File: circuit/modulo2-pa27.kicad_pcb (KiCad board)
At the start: 2 copper layers, 100 x 48 mm, 47 parts, among them J2 CONN_01X04, J3 CONN_01X04, J4 JACK_MONO, J5 HOLE, J7 HOLE, SW1 bright, U1 OPA2134, U2 OPA2134, U3 TLE2426

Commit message: further routing
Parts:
- C10, C4: footprint myAmp:C_FILM_L7.2mm_W3.5mm_P5.00mm -> myAmp:C_2.5MM
- C22, C23: footprint myAmp:C_1206 -> myAmp:C_5MM_1206
- C5: value 1n -> 250p
- C6: value 220n -> 100n
- C7: value 100n -> 47n
- R8: value 33k -> 100k
- RV1, RV2: value 50k -> 250k
- RV4: moved to B.Cu
- moved C4 12.1 mm to (94.0, 88.3)
- moved C2 9.65 mm to (109.2, 73.7), turned to 90 degrees
- moved R4 8.47 mm to (97.2, 84.5), turned to 0 degrees
- moved R7 7.18 mm to (97.2, 81.3), turned to 180 degrees
- moved R8 6.87 mm to (99.7, 72.4)
- moved C5 4.44 mm to (104.8, 73.7)
- moved C10 2.62 mm to (76.8, 85.7)
- moved C22 1.91 mm to (82.5, 92.7)
- moved C1 1.27 mm to (118.9, 81.3)
- turned RV4 to 0 degrees
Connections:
- C5 pad 2: Net-(C5-Pad2) -> /TRB
- RV1 pad 2: /TRB -> Net-(RV1-Pad2)
- RV1 pad 3: Net-(C5-Pad2) -> /TRB
- RV4 pad 3: /TRB -> Net-(RV1-Pad2)
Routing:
- net Net-(RV1-Pad2): track 0.00 -> 31.0 mm
- net Net-(R4-Pad1): track 21.1 -> 3.81 mm
- net Net-(C5-Pad2): track 16.7 -> 0.00 mm
- net /TRB: track 30.3 -> 18.1 mm
- net Net-(RV5-Pad3): track 54.1 -> 43.2 mm, vias 2 -> 1
- net Net-(C1-Pad2): track 29.5 -> 21.3 mm
- net Net-(C2-Pad2): track 53.0 -> 45.5 mm
- net /VGND: track 16.2 -> 20.6 mm, vias 0 -> 1
- net +24V: track 49.0 -> 50.8 mm
- net Net-(C4-Pad2): track 32.9 -> 31.3 mm
- net Net-(C6-Pad1): track 12.8 -> 11.2 mm
- net Net-(C10-Pad2): track 13.5 -> 12.2 mm
- net Net-(C1-Pad1): track 5.57 -> 4.30 mm
- net /VOL: track 21.1 -> 22.1 mm, vias 1 -> 0
- net Net-(C2-Pad1): track 5.19 -> 4.35 mm
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
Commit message: redone layout and tracing
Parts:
- added C24: 47u, myAmp:CPOL_D6.3_P2.5, B.Cu at (61.0, 87.0)
- added C25: 47u, myAmp:CPOL_D6.3_P2.5, B.Cu at (99.7, 76.2)
- J3, J4, RV5: moved to B.Cu
- moved R1 22.5 mm to (126.4, 94.6), turned to 0 degrees
- moved R6 19.9 mm to (110.5, 91.4), turned to 180 degrees
- moved D1 18.5 mm to (93.3, 52.1)
- moved R7 18.4 mm to (110.5, 94.0)
- moved D4 17.1 mm to (73.7, 55.9), turned to -90 degrees
- moved C3 14.1 mm to (118.1, 73.7), turned to -90 degrees
- moved R4 14.0 mm to (110.5, 88.9)
- moved R11 11.7 mm to (85.1, 80.0), turned to -90 degrees
- moved C2 11.4 mm to (109.2, 85.1), turned to 180 degrees
- moved D3 11.3 mm to (70.5, 55.9), turned to 90 degrees
- moved C23 10.9 mm to (70.5, 87.0)
- moved R14 10.0 mm to (76.2, 72.4)
- moved R18 9.88 mm to (57.8, 73.7)
- moved C22 9.25 mm to (91.4, 95.2)
- moved C8 9.09 mm to (81.9, 66.0), turned to -90 degrees
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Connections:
- J3 pad 1: /PA_OUT -> /VGND
- J3 pad 2: /VGND -> /PA_OUT
- J3 pad 3: /PA_OUT -> /VGND
- J3 pad 4: /VGND -> /PA_OUT
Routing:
- net Net-(C2-Pad2): track 45.5 -> 20.8 mm
- net Net-(D1-Pad2): track 8.89 -> 32.4 mm
- net +24V: track 50.8 -> 72.0 mm
- net Net-(RV5-Pad3): track 43.2 -> 32.9 mm, vias 1 -> 0
- net Net-(C1-Pad2): track 21.3 -> 12.1 mm
- net Net-(C3-Pad2): track 10.5 -> 19.4 mm
- net Net-(R9-Pad1): track 11.9 -> 3.17 mm
- net Net-(C4-Pad2): track 31.3 -> 39.6 mm
- net /BRT: track 7.03 -> 15.0 mm
- net GND: track 13.1 -> 6.35 mm
- net Net-(R15-Pad1): track 13.3 -> 19.8 mm
- net Net-(R13-Pad1): track 14.7 -> 8.26 mm
- net Net-(R4-Pad1): track 3.81 -> 9.90 mm
- net Net-(J4-Pad6): track 11.2 -> 6.26 mm
- net Net-(C10-Pad1): track 18.3 -> 13.8 mm
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
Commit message: made a toner transfer pa27
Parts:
- RV4: footprint myAmp:BOURNS_PTD901_xx15K -> myAmp:POT_VULGARIS
- moved D1 5.39 mm to (97.2, 55.9), turned to -90 degrees
- moved D3 3.81 mm to (66.7, 55.9)
- moved D4 3.81 mm to (69.8, 55.9)
- moved C6 1.27 mm to (101.0, 63.5)
- moved D2 0.90 mm to (94.0, 55.9), turned to 90 degrees
- moved RV1 0.11 mm to (105.0, 55.5)
- moved RV3 0.11 mm to (124.0, 55.5)
- moved RV4 0.11 mm to (81.0, 55.5)
- moved RV5 0.11 mm to (57.0, 55.5)
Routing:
- net Net-(D1-Pad2): track 32.4 -> 51.1 mm
- net /VGND: track 17.4 -> 22.2 mm
- net Net-(C6-Pad1): track 15.7 -> 14.4 mm
- net /BAS: track 55.7 -> 54.8 mm
- net /MID: track 40.3 -> 41.2 mm
- net Net-(RV1-Pad2): track 30.9 -> 30.1 mm
- net /TRB: track 21.9 -> 22.5 mm

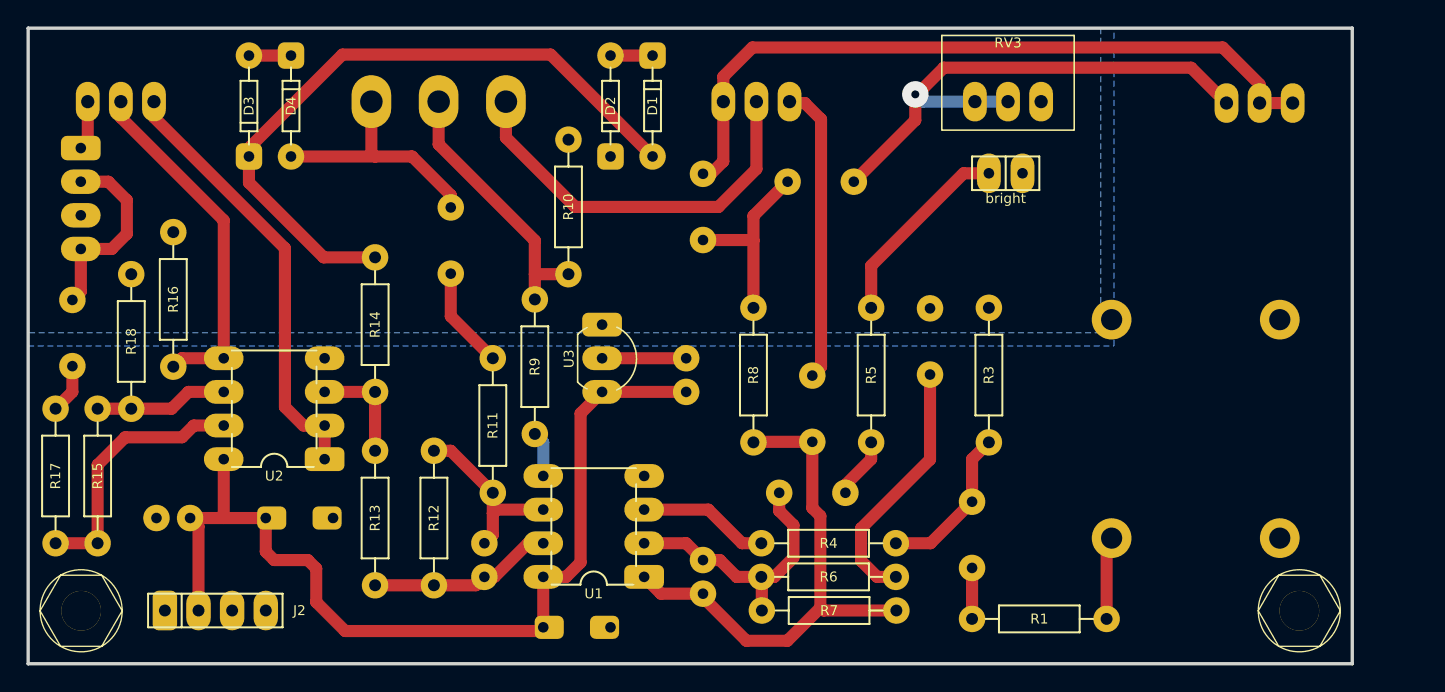
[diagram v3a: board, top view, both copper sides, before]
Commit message: made FV-1 prototype; converted kicad 5 files to kicad 6
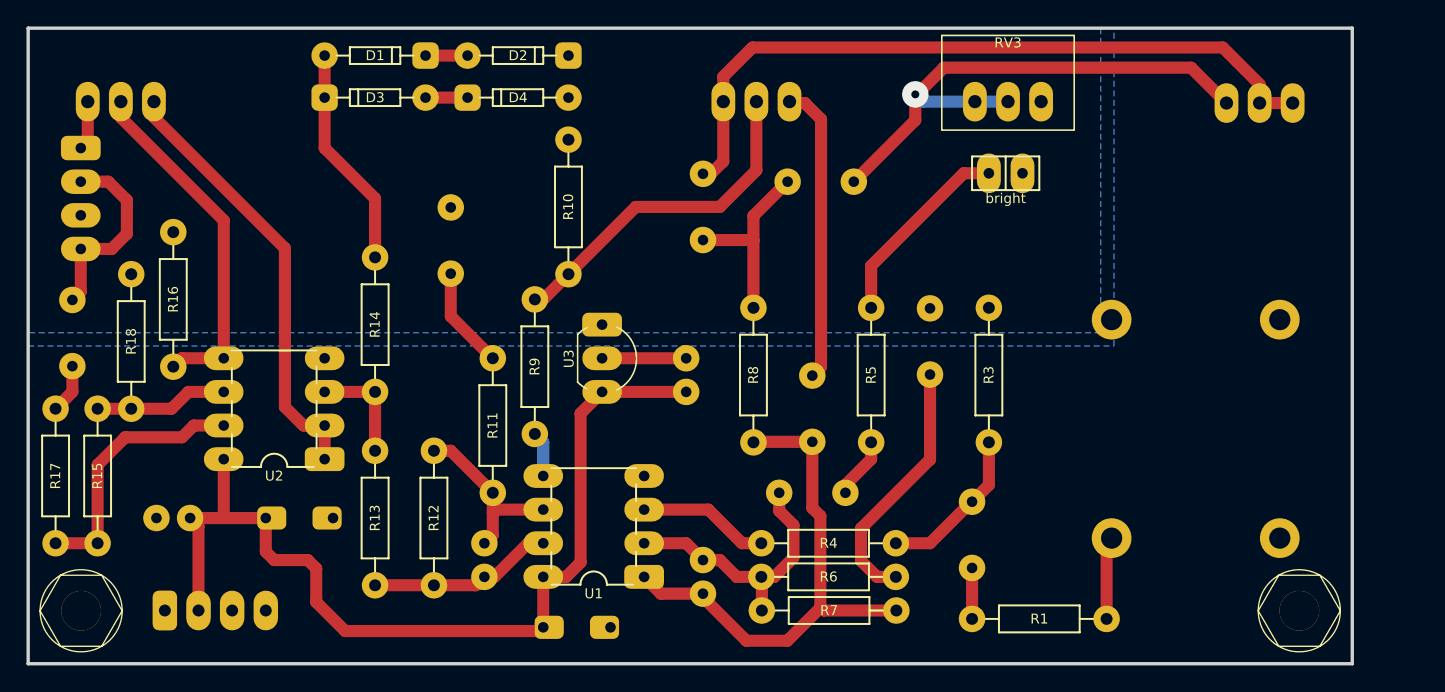
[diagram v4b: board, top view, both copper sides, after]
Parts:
- removed RV4: 500k, myAmp:POT_VULGARIS
- J2: moved to B.Cu
- R11: value 4k7 -> 10k
- R12: value 68k -> 10k
- R17: value 10k -> 220
- R7: value 68k -> 47k
- RV1, RV2: value 250k -> A250k
- RV3: value 10k -> B10k
- RV5: value 50K -> A50K
- moved D1 21.3 mm to (76.2, 52.1), turned to 180 degrees
- moved D4 17.2 mm to (87.0, 55.2), turned to 0 degrees
- moved D3 9.55 mm to (76.2, 55.2), turned to 0 degrees
- moved D2 7.96 mm to (87.0, 52.1), turned to 180 degrees
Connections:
- R10 pad 2: /VOL -> Net-(R10-Pad2)
- R9 pad 2: /VOL -> Net-(R10-Pad2)
- RV1 pad 2: Net-(RV1-Pad2) -> Net-(R10-Pad2)
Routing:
- net Net-(D1-Pad2): track 51.1 -> 16.8 mm
- net Net-(RV1-Pad2): track 30.1 -> 0.00 mm
- net Net-(R10-Pad2): track 0.00 -> 26.0 mm
- net /VOL: track 20.5 -> 0.00 mm
- net /VGND: track 22.2 -> 3.72 mm

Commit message: added report on createBanks.py; started PCB redesign
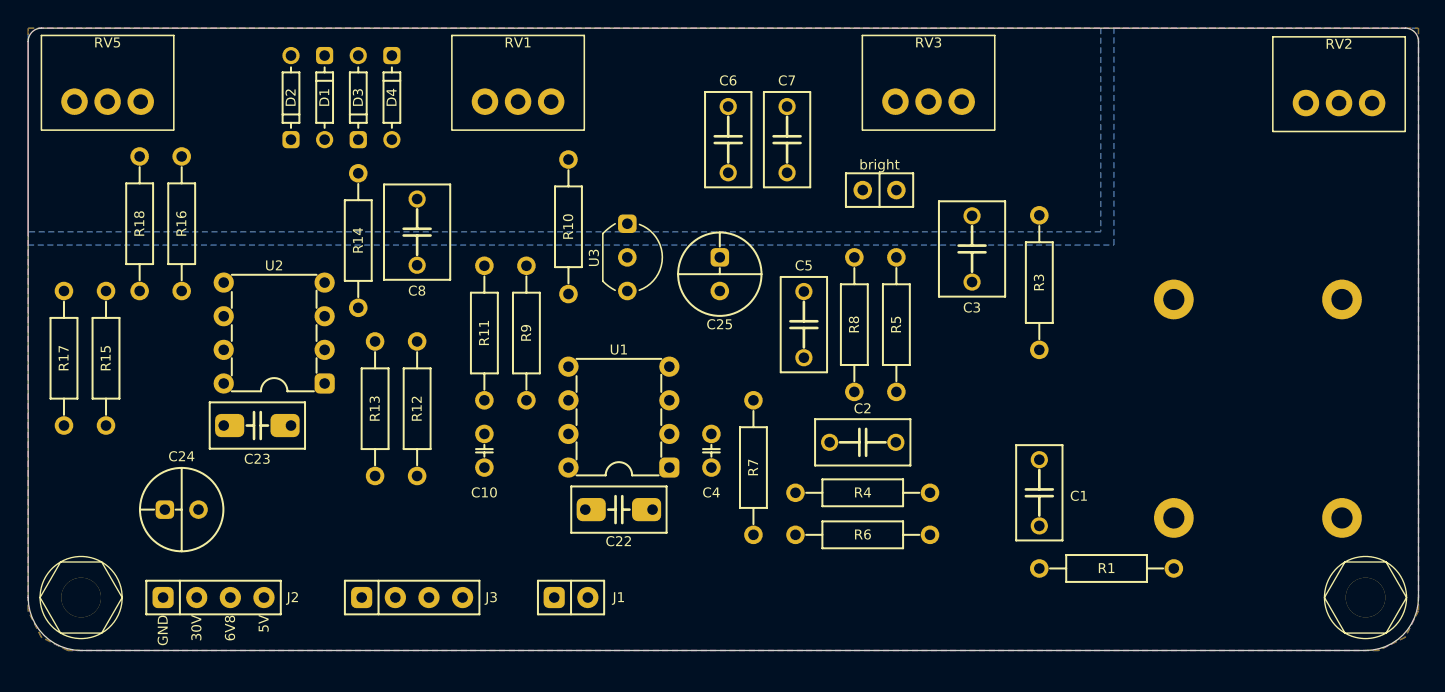
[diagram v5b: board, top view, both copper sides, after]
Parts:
- removed C11: 2u2, myAmp:C_FILM_L7.2mm_W5.5mm_P5.00mm
- added J1: CONN_01X02, myAmp:PIN_1x02, F.Cu at (91.0, 93.0)
- C1, C10, C2, C22, C23, C24, C25, C3, C4, C5, C6, C7, C8, J3, RV1, RV2, RV5: moved to F.Cu
- J2: value CONN_01X04 -> POWER; footprint myAmp:PIN_1x04 -> myAmp:POWER; moved to F.Cu
- moved J3 39.2 mm to (79.0, 93.0), turned to 0 degrees
- moved RV1 18.0 mm to (87.0, 55.5), turned to 180 degrees
- moved D2 17.4 mm to (69.8, 55.2), turned to 90 degrees
- moved R7 12.2 mm to (104.8, 83.2), turned to -90 degrees
- moved SW1 9.61 mm to (114.3, 62.2), turned to 0 degrees
- moved C4 9.55 mm to (101.6, 81.9)
- moved D4 9.53 mm to (77.5, 55.2), turned to -90 degrees
- moved C22 9.44 mm to (94.6, 86.4)
- moved R18 8.91 mm to (58.4, 64.8)
- moved R15 8.91 mm to (55.9, 74.9)
- moved R17 8.91 mm to (52.7, 74.9), turned to -90 degrees
- moved R8 8.52 mm to (112.4, 72.4)
- moved U1 8.47 mm to (94.6, 79.4)
- moved R12 8.35 mm to (79.4, 78.7)
- moved R13 8.26 mm to (76.2, 78.7)
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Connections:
- J3 pad 1: /VGND -> GND
- J3 pad 3: /VGND -> GND
- R17 pad 1: Net-(R15-Pad1) -> /PA_OUT
- R17 pad 2: Net-(C11-Pad2) -> Net-(R15-Pad1)
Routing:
- net +24V: track 72.0 -> 0.00 mm
- net /BAS: track 54.8 -> 0.00 mm
- net /MID: track 41.2 -> 0.00 mm, vias 1 -> 0
- net Net-(C4-Pad2): track 39.6 -> 0.00 mm
- net Net-(RV5-Pad3): track 33.3 -> 0.00 mm
- net Net-(R16-Pad2): track 26.7 -> 0.00 mm
- net Net-(R10-Pad2): track 26.0 -> 0.00 mm
- net /TRB: track 22.5 -> 0.00 mm
- net Net-(C2-Pad2): track 20.8 -> 0.00 mm
- net Net-(R15-Pad1): track 19.8 -> 0.00 mm
- net Net-(C3-Pad2): track 19.4 -> 0.00 mm
- net Net-(D1-Pad2): track 16.8 -> 0.00 mm
- net /BRT: track 15.0 -> 0.00 mm
- net /PA_OUT: track 14.7 -> 0.00 mm
- net Net-(C6-Pad1): track 14.4 -> 0.00 mm
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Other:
- board size 100 x 48 mm -> 105 x 47 mm

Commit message: routed pa27; routing fv-1
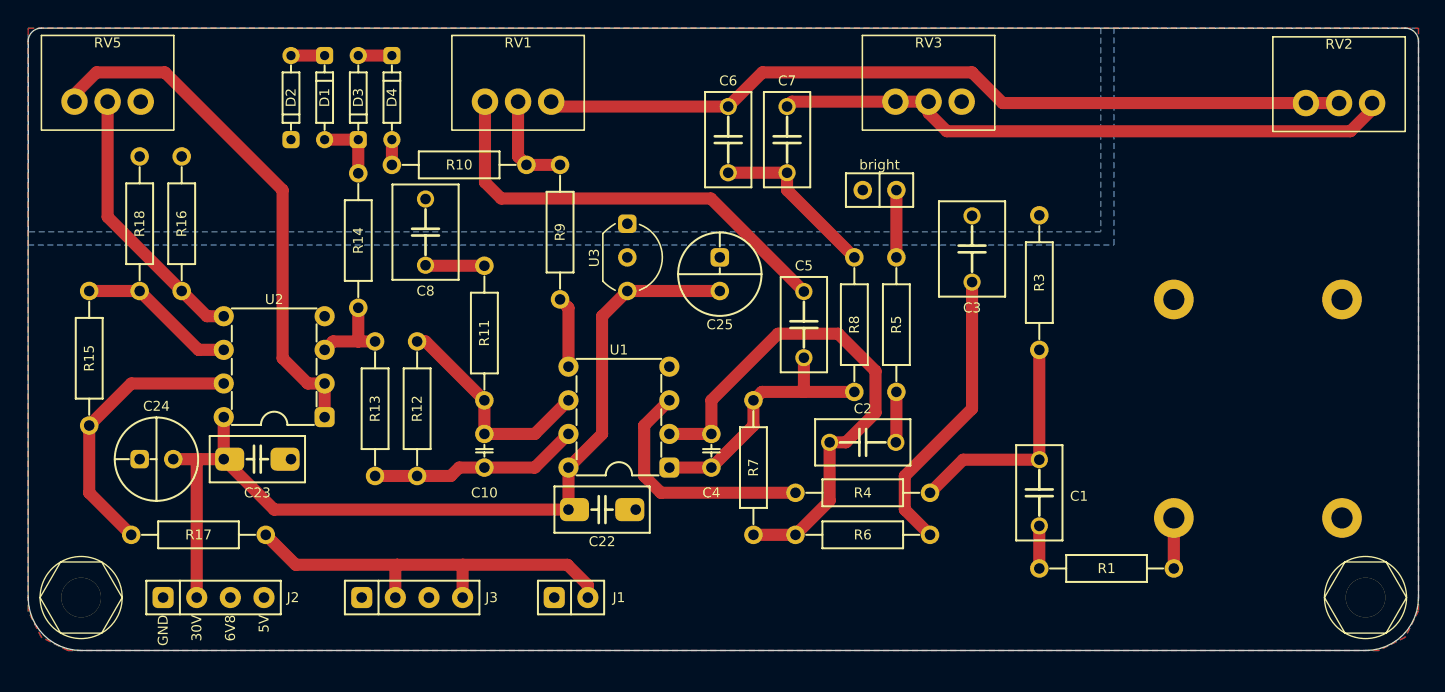
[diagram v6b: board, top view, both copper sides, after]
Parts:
- moved R17 16.8 mm to (62.9, 88.3), turned to 180 degrees
- moved R10 9.49 mm to (82.5, 60.3), turned to 0 degrees
- moved R9 8.03 mm to (90.2, 65.4)
- moved C24 4.26 mm to (59.7, 82.5)
- moved C23 2.54 mm to (67.3, 82.5)
- moved U2 2.54 mm to (68.6, 75.6)
- moved R15 1.27 mm to (54.6, 74.9)
- moved C22 1.27 mm to (93.3, 86.4)
- moved C8 0.64 mm to (80.0, 65.4)
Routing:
- net +24V: track 0.00 -> 70.4 mm
- net /BAS: track 0.00 -> 61.7 mm
- net /MID: track 0.00 -> 46.9 mm
- net Net-(C2-Pad2): track 0.00 -> 40.1 mm
- net Net-(RV5-Pad3): track 0.00 -> 39.8 mm
- net /TRB: track 0.00 -> 33.6 mm
- net /PA_OUT: track 0.00 -> 31.9 mm
- net Net-(C3-Pad2): track 0.00 -> 22.0 mm
- net Net-(R15-Pad1): track 0.00 -> 21.0 mm
- net Net-(R16-Pad2): track 0.00 -> 20.6 mm
- net Net-(C4-Pad2): track 0.00 -> 20.0 mm
- net Net-(R4-Pad1): track 0.00 -> 18.5 mm
- net Net-(C1-Pad2): track 0.00 -> 17.6 mm
- net Net-(C10-Pad1): track 0.00 -> 16.9 mm
- net Net-(C10-Pad2): track 0.00 -> 15.9 mm
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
